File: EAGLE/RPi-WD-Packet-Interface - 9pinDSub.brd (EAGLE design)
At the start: 68.2 x 40.6 mm, 21 parts, among them IC1 TLC555, T1 2N3904, T2 2N3904, T3 2N3904

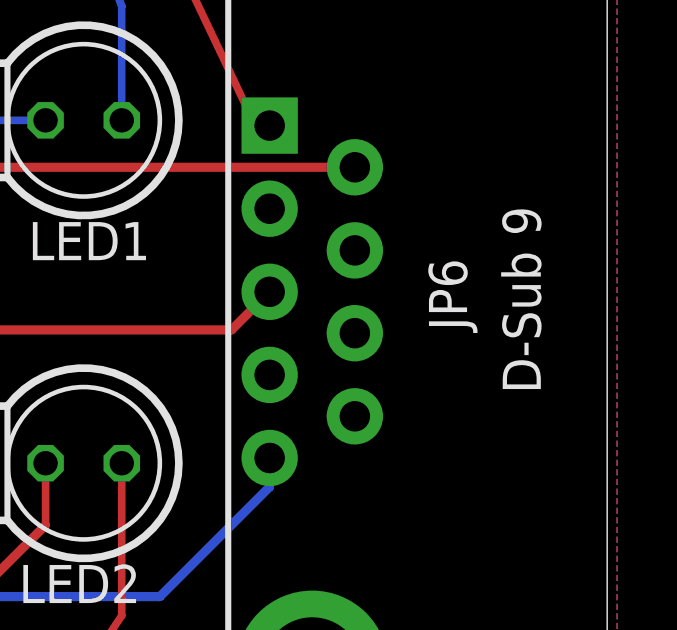
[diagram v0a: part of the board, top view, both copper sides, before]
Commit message: Update JP part numbers, new BOM export
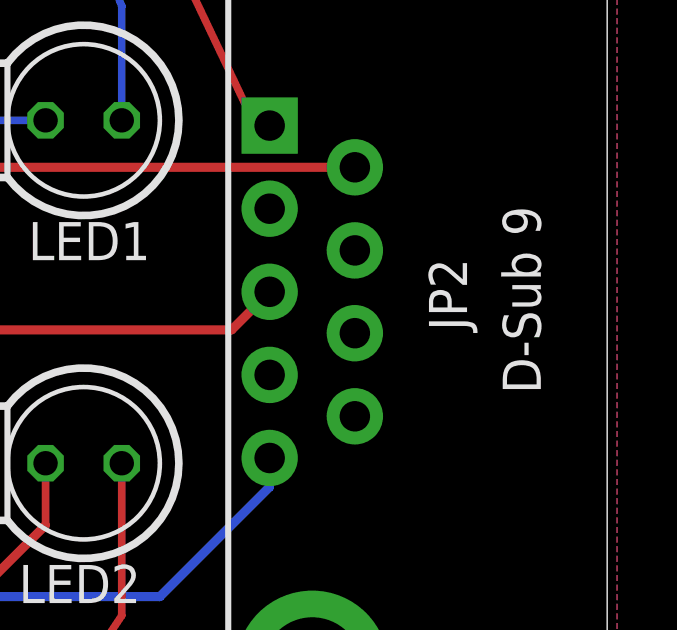
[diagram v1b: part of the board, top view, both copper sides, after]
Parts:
- renumbered JP6 to JP2
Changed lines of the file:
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@@
 <attribute name="NAME" x="2.2225" y="27.94" size="1.27" layer="25" rot="R90"/>
 </element>
-<element name="JP6" library="SparkFun-Connectors" package="DB9" value="Radio" x="58.42" y="20.32" smashed="yes" rot="R270">
+<element name="JP2" library="SparkFun-Connectors" package="DB9" value="Radio" x="58.42" y="20.32" smashed="yes" rot="R270">
 <attribute name="PROD_ID" value="CONN-08194" x="58.42" y="20.32" size="1.778" layer="27" rot="R270" display="off"/>
 <attribute name="NAME" x="62.31" y="21.4325" size="1.27" layer="25" ratio="10" rot="R270"/>
@@
 <signal name="PTT">
 <contactref element="T1" pad="1"/>
-<contactref element="JP6" pad="3"/>
+<contactref element="JP2" pad="3"/>
 <wire x1="56.99125" y1="20.32" x2="57" y2="20.32" width="0.254" layer="1"/>
 <wire x1="44.45" y1="19.05" x2="55.73" y2="19.05" width="0.3048" layer="1"/>
@@
 </signal>
 <signal name="TXAUDIO">
-<contactref element="JP6" pad="1"/>
+<contactref element="JP2" pad="1"/>
 <contactref element="C4" pad="2"/>
 <wire x1="20.955" y1="30.00375" x2="20.955" y2="29.21" width="0.254" layer="1"/>
@@
 </signal>
 <signal name="RXAUDIO">
-<contactref element="JP6" pad="5"/>
+<contactref element="JP2" pad="5"/>
 <contactref element="JP3" pad="TIP"/>
 <wire x1="8.89" y1="6.50875" x2="39.6875" y2="6.50875" width="0.254" layer="16"/>
@@
 <contactref element="JP1" pad="1"/>
 <contactref element="T3" pad="3"/>
-<contactref element="JP6" pad="6"/>
+<contactref element="JP2" pad="6"/>
 <contactref element="JP4" pad="SLEEVE"/>
 <wire x1="39.37" y1="26.19375" x2="39.21125" y2="26.035" width="0.254" layer="16"/>

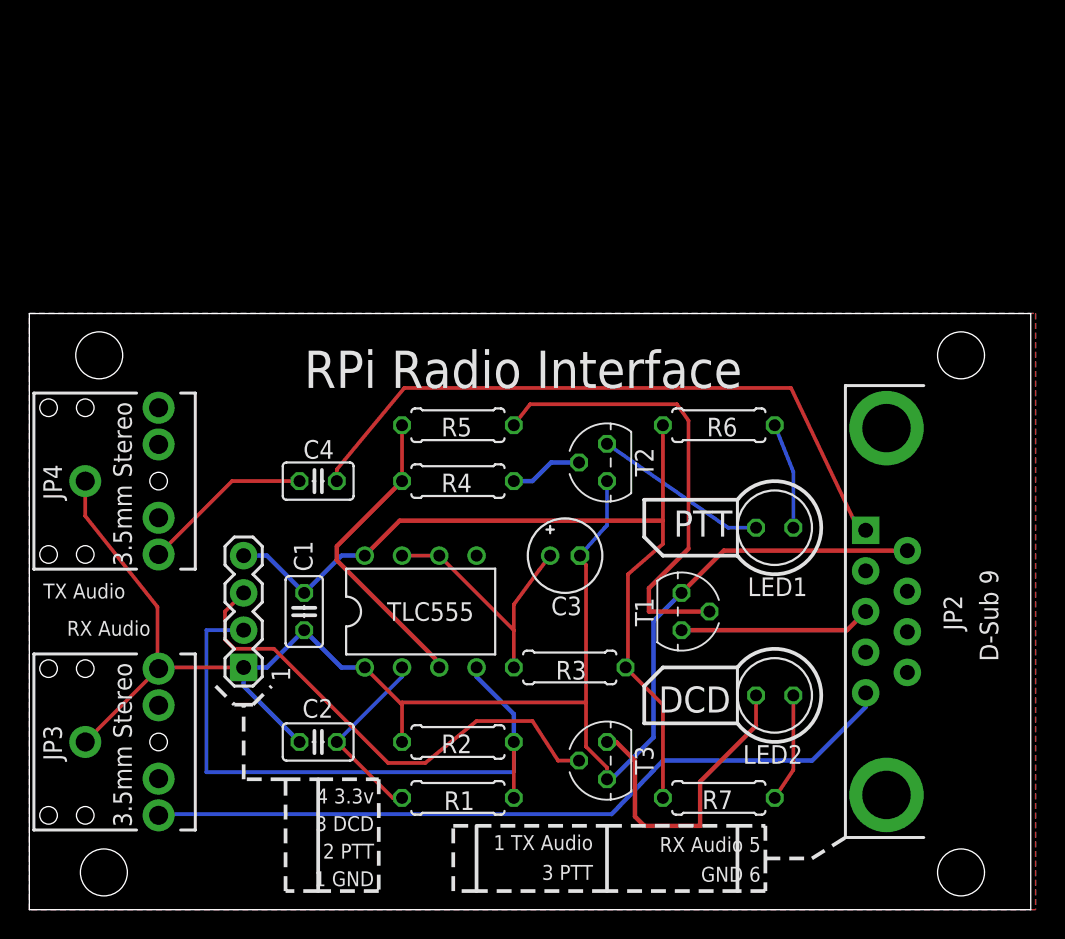
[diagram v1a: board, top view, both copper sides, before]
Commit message: Updates after first assembly
Added DCD LED bias resistor, text, widened board for additional mount
hole clearance.
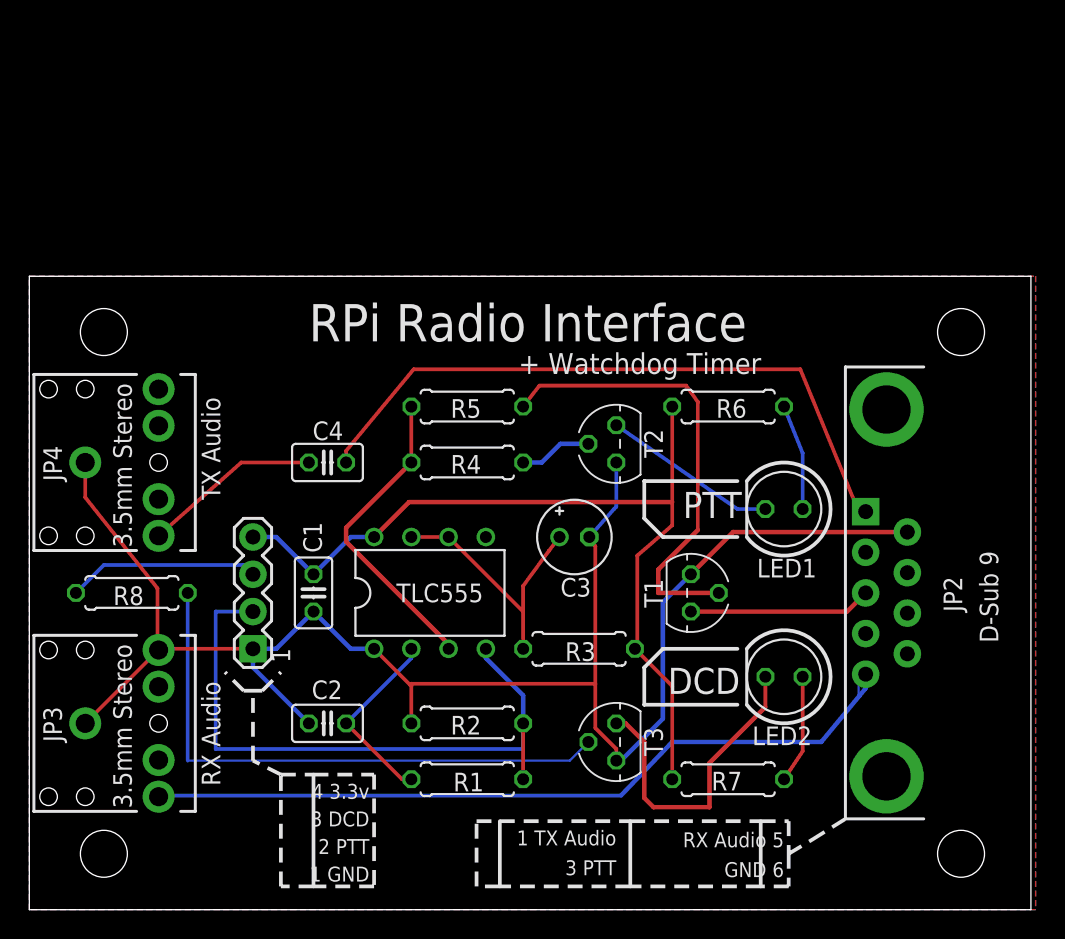
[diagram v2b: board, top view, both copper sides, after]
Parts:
- added R8: 3K, rcl:0207/7
- moved LED1 1.42 mm to (51.4, 27.3)
- moved LED2 1.42 mm to (51.4, 15.9)
- moved R3 1.42 mm to (37.5, 17.8)
- moved T2 1.42 mm to (40.0, 31.8)
- moved T3 1.42 mm to (40.0, 11.4)
- moved C2 1.42 mm to (20.3, 12.7)
- moved C4 1.42 mm to (20.3, 30.5)
- moved JP1 1.42 mm to (15.2, 17.8)
- moved R1 1.42 mm to (29.8, 8.89)
- moved R7 1.42 mm to (47.6, 8.89)
- moved C1 1.42 mm to (19.4, 21.6)
- moved C3 1.42 mm to (37.1, 25.4)
- moved IC1 1.42 mm to (27.3, 21.6)
- moved R2 1.42 mm to (29.8, 12.7)
- moved R4 1.42 mm to (29.8, 30.5)
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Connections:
- new net N$10: R8.2, T3.2
- net GPIO-DCD: now also R8.1; no longer T3.2
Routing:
- net N$10: track 0.00 -> 39.3 mm
- net GPIO-DCD: track 33.8 -> 13.1 mm
- net RXAUDIO: track 52.2 -> 54.3 mm
- net GPIO-PTT: track 45.2 -> 44.5 mm
- net PTT: track 13.1 -> 12.4 mm
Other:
- board size 68.2 x 40.6 mm -> 68.3 x 43.2 mm
- board text added: "+ Watchdog Timer"
- board text added: "https://github.com/jaymzx/RPi-WD-Packet-Interface"
- board text added: "v1.1"

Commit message: Design update to v1.1
Added channel selection jumpers for RX/TX, single-line PTT resistor
jumper, TX audio level pot, timeout delay pot (0-2 mins /w specified
values). Moved to Dangerous Prototypes 'Sick of Beige' 60mm x 60mm PCB
layout standard.
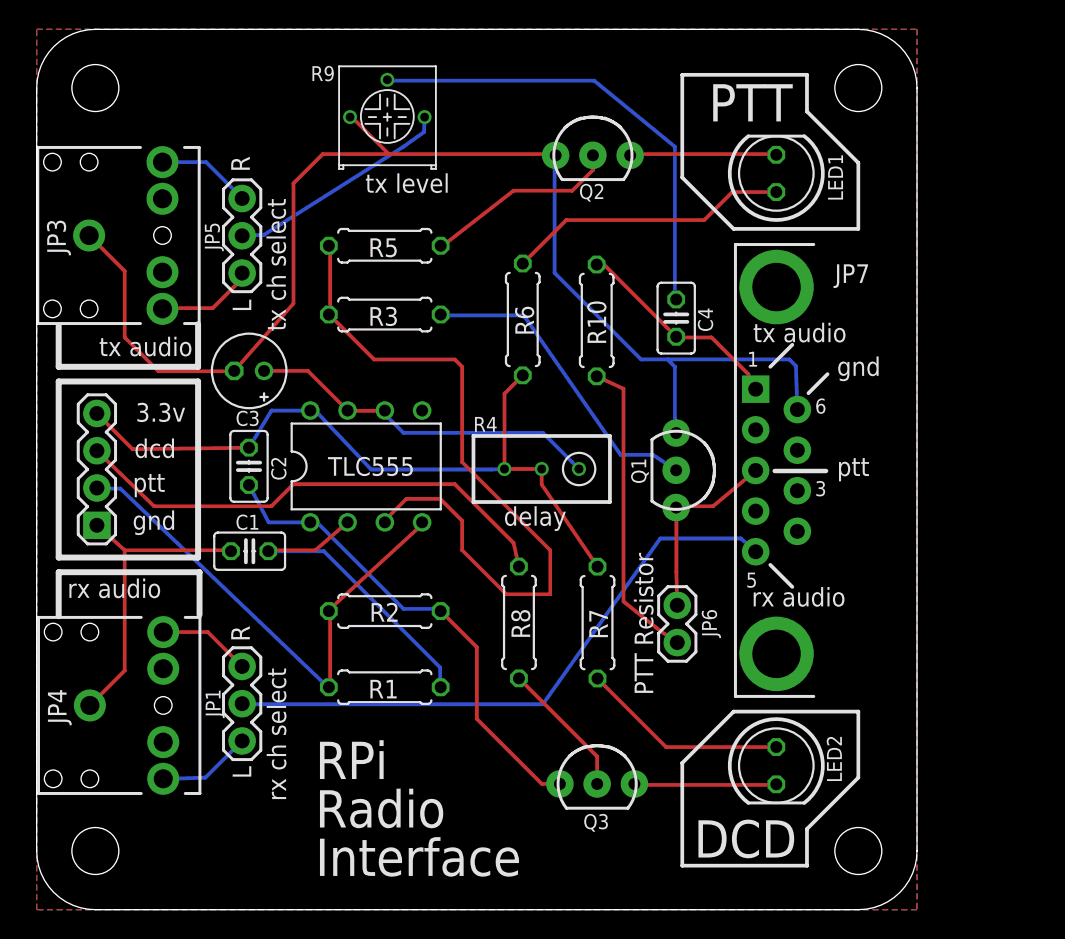
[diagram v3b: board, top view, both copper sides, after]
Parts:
- removed T1, T2, T3: 2N3904, transistor:TO92
- added JP5: tx ch select, SparkFun-Connectors:1X03
- added JP6: PTT Resistor Enable, SparkFun-Connectors:1X02
- added JP7: Radio, SparkFun-Connectors:DB9
- added PCB1: PCB_DP_SQUARE-6X6, dp_devices:DP6060_V1
- added Q1: PTT, SparkFun-DiscreteSemi:TO-92-AMMO
- added Q2: PTT-LED, SparkFun-DiscreteSemi:TO-92-AMMO
- added Q3: DCD-LED, SparkFun-DiscreteSemi:TO-92-AMMO
- added R10: 2.2K, rcl:0207/7
- added R9: 10K, GeekAmmo:RTRIM3362P
- C3: value 10 -> 100
- JP1: value RPi -> rx ch select; device SparkFun-Connectors:1X04 -> SparkFun-Connectors:1X03
- JP2: value Radio -> RPi; device SparkFun-Connectors:DB9 -> SparkFun-Connectors:1X04
- JP3: value RX Audio -> TX Audio
- JP4: value TX Audio -> RX Audio
- R3: value 1M -> 3K
- R4: value 3K -> 1M; device rcl:0207/7 -> rcl:RTRIM3296W
- R6, R7: value 68 -> 100
- moved JP2 54.0 mm to (4.61, 26.2), turned to 90 degrees
- moved JP3 33.3 mm to (4.08, 46.0)
- moved R8 26.5 mm to (33.4, 19.6), turned to 270 degrees
- moved R3 26.3 mm to (24.2, 40.6), turned to 180 degrees
- moved C4 25.7 mm to (44.1, 40.3), turned to 270 degrees
- moved C3 24.9 mm to (15.0, 36.7), turned to 180 degrees
- moved LED1 22.9 mm to (50.9, 50.2), turned to 90 degrees
- moved C2 18.3 mm to (15.0, 30.2), turned to 270 degrees
- moved JP4 16.6 mm to (4.12, 13.9)
- moved R6 15.2 mm to (33.6, 40.2), turned to 270 degrees
- moved R7 13.9 mm to (38.7, 19.6), turned to 90 degrees
- moved R5 12.3 mm to (24.2, 45.2)
- moved IC1 9.65 mm to (23.0, 30.2)
- moved R2 9.49 mm to (24.2, 20.4), turned to 0 degrees
- moved R1 8.42 mm to (24.2, 15.2), turned to 180 degrees
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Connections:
- new net N$11: JP6.2, R10.2
- new net RXAUD-L: JP1.1, JP4.TIP
- new net RXAUD-R: JP1.3, JP4.RING
- new net TXAUD-L: JP3.TIP, JP5.1
- new net TXAUD-R: JP3.RING, JP5.3
- new net TXAUDIO-HOT: JP5.2, R9.3
- net GND: now also JP2.1, JP7.6, Q1.1, Q2.1, Q3.1, R9.1; no longer JP1.1, JP2.6, JP3.RING, T1.3, T2.3, T3.3
- net GPIO-DCD: now also JP2.3; no longer JP1.3
- net GPIO-PTT: now also JP2.2; no longer JP1.2
- net N$10: now also Q3.2; no longer T3.2
- net N$3: now also C1.1; no longer C2.1
- net N$4: now also R9.2; no longer JP4.TIP
- net N$5: now also R4.1; no longer R3.1
- net N$6: now also Q2.3; no longer T2.1
- net N$7: now also Q2.2, R5.1; no longer R4.1, T2.2
- net N$8: now also Q1.2, R3.1; no longer R5.1, T1.2
- net N$9: now also Q3.3; no longer T3.1
- net PTT: now also JP6.1, JP7.3, Q1.3; no longer JP2.3, T1.1
- net PTT_TRIGGER: now also R3.2; no longer R4.2
- net RXAUDIO: now also JP1.2, JP7.5; no longer JP2.5, JP3.TIP
- net TXAUDIO: now also JP7.1, R10.1; no longer JP2.1
- net VCC: now also C2.1, JP2.4, R4.2, R4.3; no longer C1.1, JP1.4, R3.2
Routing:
- net TXAUDIO: track 45.3 -> 14.7 mm
- net N$10: track 39.3 -> 9.41 mm
- net PTT_TRIGGER: track 21.2 -> 49.1 mm
- net GND: track 116.5 -> 143.0 mm
- net N$11: track 0.00 -> 21.1 mm
- net GPIO-DCD: track 13.1 -> 33.9 mm
- net N$4: track 12.1 -> 31.6 mm
- net TXAUDIO-HOT: track 0.00 -> 15.5 mm
- net RXAUDIO: track 54.3 -> 41.2 mm
- net N$1: track 7.23 -> 19.3 mm
- net N$9: track 21.4 -> 9.68 mm
- net N$8: track 31.4 -> 21.3 mm
- net VCC: track 59.4 -> 49.5 mm
- net N$3: track 12.9 -> 22.5 mm
- net GPIO-PTT: track 44.5 -> 35.2 mm
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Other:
- board size 68.3 x 43.2 mm -> 60 x 60 mm
- board text added: "3"
- board text added: "3.3v"
- board text added: "5"
- board text added: "6"
- board text added: "L"
- board text added: "PTT Resistor"
- board text added: "R"
- board text added: "dcd"
- board text added: "delay"
- board text added: "github.com/jaymzx/RPi-WD-Packet-Interface"
- board text added: "gnd"
- board text added: "ptt"
- board text added: "rx audio"
- board text added: "tx audio"
- board text added: "tx level"
- board text added: "version 1.1"
- board text removed: "+ Watchdog Timer"
- board text removed: "1 TX Audio 3 PTT"
- board text removed: "3.5mm Stereo"
- board text removed: "4 3.3v 3 DCD 2 PTT 1 GND"
- board text removed: "D-Sub 9"
- board text removed: "RX Audio"
- board text removed: "RX Audio 5 GND 6"
- board text removed: "TX Audio"
- board text removed: "https://github.com/jaymzx/RPi-WD-Packet-Interface"
- board text removed: "v1.1"

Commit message: Update PCB to v1.1a, add images of board and schematic
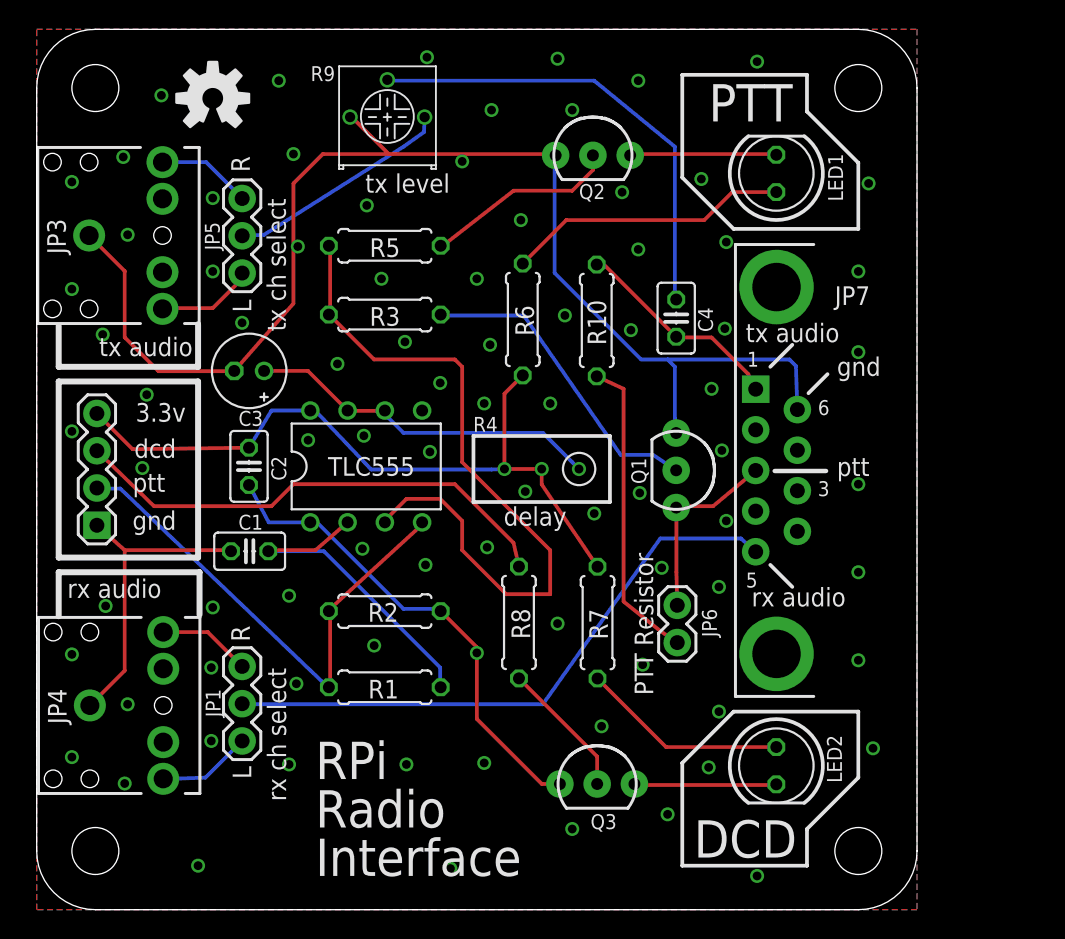
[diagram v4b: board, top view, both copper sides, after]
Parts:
- added LOGO1: OSHW-LOGOM, SparkFun-Aesthetics:OSHW-LOGO-M
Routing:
- net GND: vias 0 -> 85
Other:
- board text added: "version 1.1 rev A"
- board text removed: "version 1.1"

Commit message: Update repo to board revision B
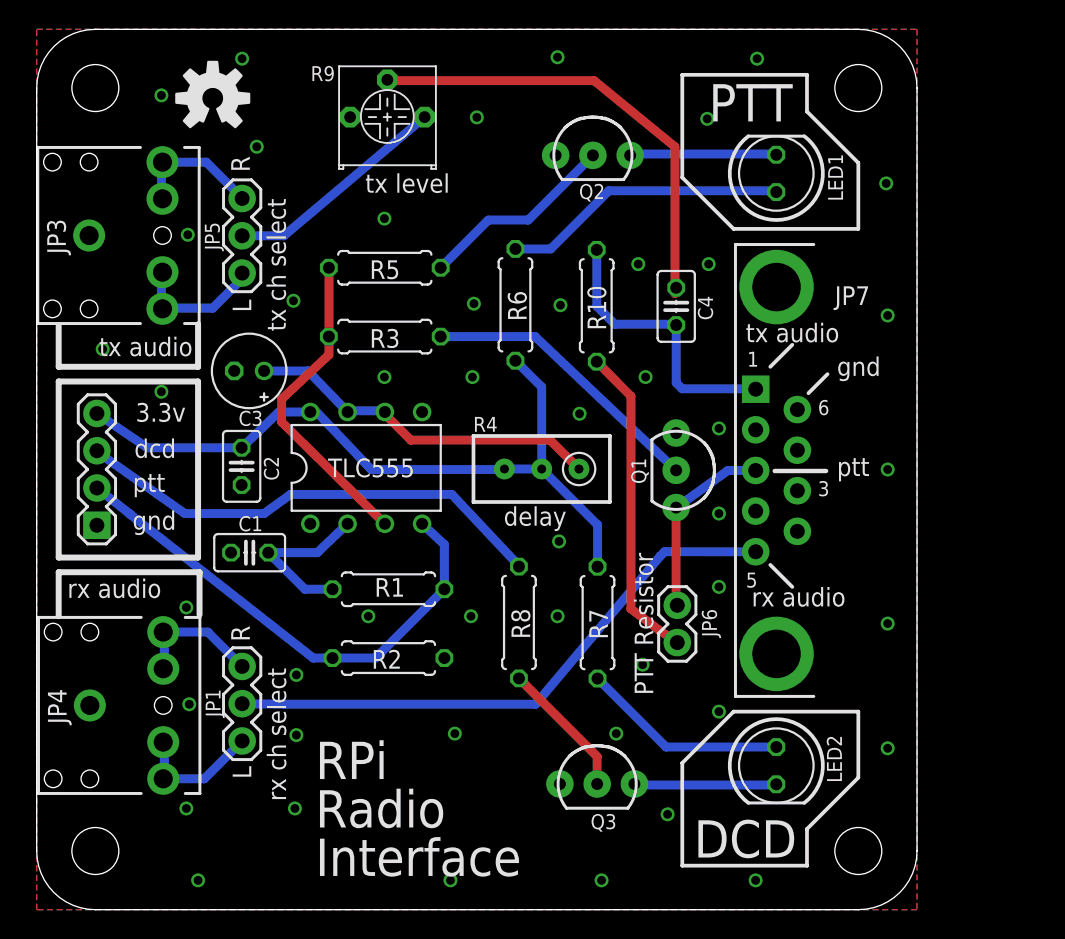
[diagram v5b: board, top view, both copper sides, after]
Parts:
- moved R1 6.68 mm to (24.5, 21.8), turned to 0 degrees
- moved R2 3.21 mm to (24.5, 17.1)
- moved R3 1.50 mm to (24.2, 39.1)
- moved R5 1.50 mm to (24.2, 43.8)
- moved R6 1.12 mm to (33.1, 41.2)
- moved R10 1.00 mm to (38.7, 41.2)
- moved C4 0.80 mm to (44.1, 41.1)
- moved C2 0.50 mm to (14.5, 30.2)
- moved C1 0.10 mm to (15.0, 24.3)
- moved IC1 0.10 mm to (23.0, 30.1)
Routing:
- net GND: track 143.0 -> 0.00 mm, vias 85 -> 47
- net PTT_TRIGGER: track 49.1 -> 21.8 mm
- net N$3: track 22.5 -> 11.6 mm
- net TXAUDIO: track 14.7 -> 19.3 mm
- net N$12: track 0.00 -> 3.00 mm
- net N$15: track 0.00 -> 2.50 mm
- net N$14: track 0.00 -> 2.50 mm
- net N$13: track 0.00 -> 2.50 mm
- net N$8: track 21.3 -> 19.7 mm
- net RXAUDIO: track 41.2 -> 39.8 mm
- net VCC: track 49.5 -> 50.6 mm
- net GPIO-DCD: track 33.9 -> 33.0 mm
- net N$11: track 21.1 -> 21.7 mm
- net TXAUD-R: track 6.47 -> 6.44 mm, vias 1 -> 0
- net RXAUD-L: track 6.47 -> 6.45 mm, vias 2 -> 0
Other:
- board text added: "version 1.1 rev B"
- board text removed: "version 1.1 rev A"
